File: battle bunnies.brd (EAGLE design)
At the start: 151.7 x 94 mm, 59 parts, among them IC1 CP2104, Q1 mmbt2222, Q2 mmbt2222, SW2 KMR2, U1 PCA9685, U2 SPX3819, U3 MCP73831T-2ACI/OT, X2 ESP-12, X4 20329

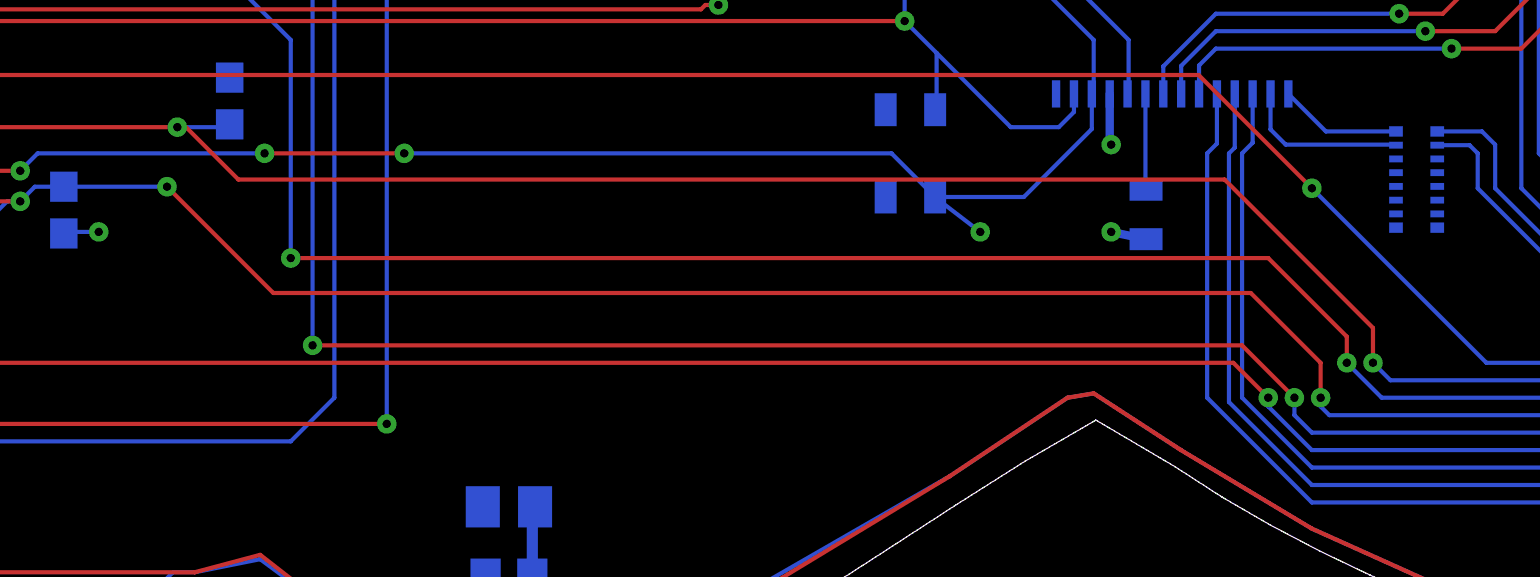
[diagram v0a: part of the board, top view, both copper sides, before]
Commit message: Fixing the trace that ran through the exposed ear
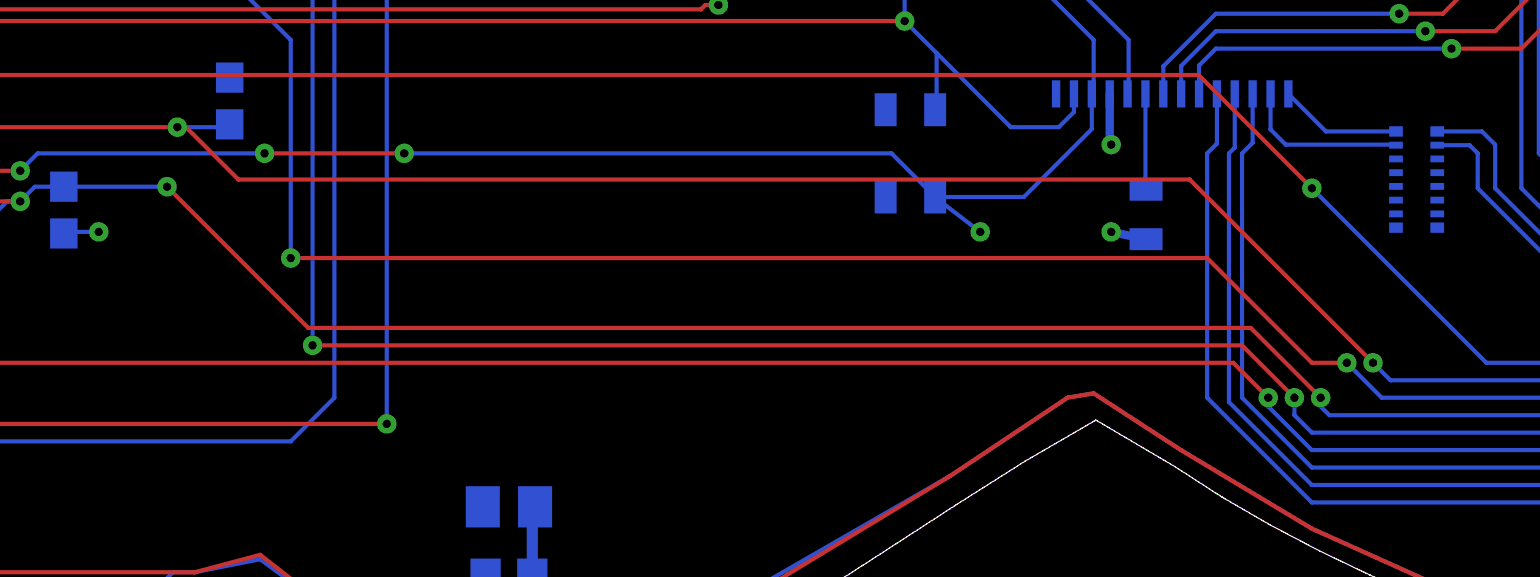
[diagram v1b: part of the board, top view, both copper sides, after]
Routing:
- net GPIO15: track 127.3 -> 126.6 mm
- net GPIO2: track 102.9 -> 102.2 mm
- net RESET: track 153.2 -> 152.6 mm
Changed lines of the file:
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@@
 <layer number="155" name="FabDoc3" color="7" fill="1" visible="yes" active="yes"/>
 <layer number="199" name="Contour" color="7" fill="1" visible="yes" active="yes"/>
-<layer number="200" name="200bmp" color="1" fill="10" visible="no" active="yes"/>
-<layer number="201" name="201bmp" color="2" fill="10" visible="no" active="yes"/>
-<layer number="202" name="202bmp" color="3" fill="10" visible="no" active="yes"/>
-<layer number="203" name="203bmp" color="4" fill="10" visible="no" active="yes"/>
-<layer number="204" name="204bmp" color="5" fill="10" visible="no" active="yes"/>
-<layer number="205" name="205bmp" color="6" fill="10" visible="no" active="yes"/>
-<layer number="206" name="206bmp" color="7" fill="10" visible="no" active="yes"/>
-<layer number="207" name="207bmp" color="8" fill="10" visible="no" active="yes"/>
-<layer number="208" name="208bmp" color="9" fill="10" visible="no" active="yes"/>
-<layer number="209" name="209bmp" color="10" fill="10" visible="no" active="yes"/>
-<layer number="210" name="210bmp" color="11" fill="10" visible="no" active="yes"/>
-<layer number="211" name="211bmp" color="12" fill="10" visible="no" active="yes"/>
-<layer number="212" name="212bmp" color="13" fill="10" visible="no" active="yes"/>
-<layer number="213" name="213bmp" color="14" fill="10" visible="no" active="yes"/>
-<layer number="214" name="214bmp" color="15" fill="10" visible="no" active="yes"/>
-<layer number="215" name="215bmp" color="16" fill="10" visible="no" active="yes"/>
-<layer number="216" name="216bmp" color="7" fill="1" visible="no" active="yes"/>
+<layer number="200" name="200bmp" color="1" fill="10" visible="yes" active="yes"/>
+<layer number="201" name="201bmp" color="2" fill="10" visible="yes" active="yes"/>
+<layer number="202" name="202bmp" color="3" fill="10" visible="yes" active="yes"/>
+<layer number="203" name="203bmp" color="4" fill="10" visible="yes" active="yes"/>
+<layer number="204" name="204bmp" color="5" fill="10" visible="yes" active="yes"/>
+<layer number="205" name="205bmp" color="6" fill="10" visible="yes" active="yes"/>
+<layer number="206" name="206bmp" color="7" fill="10" visible="yes" active="yes"/>
+<layer number="207" name="207bmp" color="8" fill="10" visible="yes" active="yes"/>
+<layer number="208" name="208bmp" color="9" fill="10" visible="yes" active="yes"/>
+<layer number="209" name="209bmp" color="10" fill="10" visible="yes" active="yes"/>
+<layer number="210" name="210bmp" color="11" fill="10" visible="yes" active="yes"/>
+<layer number="211" name="211bmp" color="12" fill="10" visible="yes" active="yes"/>
+<layer number="212" name="212bmp" color="13" fill="10" visible="yes" active="yes"/>
+<layer number="213" name="213bmp" color="14" fill="10" visible="yes" active="yes"/>
+<layer number="214" name="214bmp" color="15" fill="10" visible="yes" active="yes"/>
+<layer number="215" name="215bmp" color="16" fill="10" visible="yes" active="yes"/>
+<layer number="216" name="216bmp" color="7" fill="1" visible="yes" active="yes"/>
 <layer number="217" name="217bmp" color="18" fill="1" visible="no" active="no"/>
 <layer number="218" name="218bmp" color="19" fill="1" visible="no" active="no"/>
@@
 <layer number="223" name="223bmp" color="24" fill="1" visible="no" active="no"/>
 <layer number="224" name="224bmp" color="25" fill="1" visible="no" active="no"/>
-<layer number="225" name="225bmp" color="7" fill="1" visible="no" active="yes"/>
-<layer number="226" name="226bmp" color="7" fill="1" visible="no" active="yes"/>
-<layer number="227" name="227bmp" color="7" fill="1" visible="no" active="yes"/>
-<layer number="228" name="228bmp" color="7" fill="1" visible="no" active="yes"/>
-<layer number="229" name="229bmp" color="7" fill="1" visible="no" active="yes"/>
-<layer number="230" name="230bmp" color="7" fill="1" visible="no" active="yes"/>
-<layer number="231" name="231bmp" color="7" fill="1" visible="no" active="yes"/>
+<layer number="225" name="225bmp" color="7" fill="1" visible="yes" active="yes"/>
+<layer number="226" name="226bmp" color="7" fill="1" visible="yes" active="yes"/>
+<layer number="227" name="227bmp" color="7" fill="1" visible="yes" active="yes"/>
+<layer number="228" name="228bmp" color="7" fill="1" visible="yes" active="yes"/>
+<layer number="229" name="229bmp" color="7" fill="1" visible="yes" active="yes"/>
+<layer number="230" name="230bmp" color="7" fill="1" visible="yes" active="yes"/>
+<layer number="231" name="231bmp" color="7" fill="1" visible="yes" active="yes"/>
 <layer number="232" name="Eagle3D_PG2" color="7" fill="1" visible="no" active="no"/>
 <layer number="233" name="Eagle3D_PG3" color="7" fill="1" visible="no" active="no"/>
-<layer number="248" name="Housing" color="7" fill="1" visible="no" active="yes"/>
-<layer number="249" name="Edge" color="7" fill="1" visible="no" active="yes"/>
+<layer number="248" name="Housing" color="7" fill="1" visible="yes" active="yes"/>
+<layer number="249" name="Edge" color="7" fill="1" visible="yes" active="yes"/>
 <layer number="250" name="Descript" color="3" fill="1" visible="no" active="no"/>
 <layer number="251" name="SMDround" color="12" fill="11" visible="no" active="no"/>
-<layer number="254" name="cooling" color="7" fill="1" visible="no" active="yes"/>
-<layer number="255" name="routoute" color="7" fill="1" visible="no" active="yes"/>
+<layer number="254" name="cooling" color="7" fill="1" visible="yes" active="yes"/>
+<layer number="255" name="routoute" color="7" fill="1" visible="yes" active="yes"/>
 </layers>
 <board>
@@
 <wire x1="34.0925" y1="68.9525" x2="34.355" y2="69.215" width="0.1524" layer="1"/>
 <wire x1="55.245" y1="69.215" x2="45.4025" y2="69.215" width="0.1524" layer="16"/>
-<wire x1="100.33" y1="51.7525" x2="100.33" y2="50.8" width="0.1524" layer="1"/>
 <via x="100.33" y="50.8" extent="1-16" drill="0.3048" diameter="0.3048"/>
 <wire x1="100.33" y1="50.8" x2="101.6" y2="49.53" width="0.1524" layer="16"/>
 <wire x1="137.16" y1="44.45" x2="137.16" y2="41.91" width="0.1524" layer="16"/>
-<wire x1="61.9125" y1="54.61" x2="97.4725" y2="54.61" width="0.1524" layer="1"/>
-<wire x1="97.4725" y1="54.61" x2="100.33" y2="51.7525" width="0.1524" layer="1"/>
+<wire x1="61.9125" y1="54.61" x2="95.25" y2="54.61" width="0.1524" layer="1"/>
 <wire x1="101.6" y1="49.53" x2="128.27" y2="49.53" width="0.1524" layer="16"/>
 <wire x1="128.27" y1="49.53" x2="132.08" y2="45.72" width="0.1524" layer="16"/>
 <wire x1="132.08" y1="45.72" x2="135.89" y2="45.72" width="0.1524" layer="16"/>
 <wire x1="135.89" y1="45.72" x2="137.16" y2="44.45" width="0.1524" layer="16"/>
+<wire x1="100.33" y1="50.8" x2="99.06" y2="50.8" width="0.1524" layer="1"/>
+<wire x1="99.06" y1="50.8" x2="95.25" y2="54.61" width="0.1524" layer="1"/>
 </signal>
 <signal name="ADC">
@@
 <contactref element="JP2" pad="7"/>
 <wire x1="49.29" y1="57.15" x2="49.0925" y2="56.9525" width="0.1524" layer="1"/>
-<wire x1="99.3775" y1="50.8" x2="99.3775" y2="49.53" width="0.1524" layer="1"/>
 <via x="99.3775" y="49.53" extent="1-16" drill="0.3048" diameter="0.3048"/>
 <wire x1="99.3775" y1="49.53" x2="99.3775" y2="49.2125" width="0.1524" layer="16"/>
 <wire x1="99.3775" y1="49.2125" x2="99.695" y2="48.895" width="0.1524" layer="16"/>
-<wire x1="61.2775" y1="53.34" x2="96.8375" y2="53.34" width="0.1524" layer="1"/>
-<wire x1="96.8375" y1="53.34" x2="99.3775" y2="50.8" width="0.1524" layer="1"/>
 <wire x1="99.695" y1="48.895" x2="127.635" y2="48.895" width="0.1524" layer="16"/>
 <wire x1="127.635" y1="48.895" x2="132.08" y2="44.45" width="0.1524" layer="16"/>
-<wire x1="61.2775" y1="53.34" x2="57.41125" y2="57.20625" width="0.1524" layer="1"/>
+<wire x1="62.5475" y1="52.07" x2="57.41125" y2="57.20625" width="0.1524" layer="1"/>
 <wire x1="49.29" y1="57.15" x2="49.76625" y2="56.67375" width="0.1524" layer="1"/>
 <via x="52.07" y="56.67375" extent="1-16" drill="0.3048" diameter="0.3048"/>
@@
 <wire x1="45.72" y1="50.8" x2="51.59375" y2="56.67375" width="0.1524" layer="16"/>
 <wire x1="51.59375" y1="56.67375" x2="52.07" y2="56.67375" width="0.1524" layer="16"/>
+<wire x1="62.5475" y1="52.07" x2="96.8375" y2="52.07" width="0.1524" layer="1"/>
+<wire x1="96.8375" y1="52.07" x2="99.3775" y2="49.53" width="0.1524" layer="1"/>
 </signal>
 <signal name="GPIO0">
@@
 <wire x1="59.5875" y1="59.3725" x2="59.69" y2="59.475" width="0.1524" layer="16"/>
 <contactref element="JP2" pad="4"/>
-<wire x1="95.885" y1="57.4675" x2="60.0075" y2="57.4675" width="0.1524" layer="1"/>
+<wire x1="94.615" y1="57.4675" x2="60.0075" y2="57.4675" width="0.1524" layer="1"/>
 <wire x1="60.0075" y1="57.4675" x2="58.1025" y2="59.3725" width="0.1524" layer="1"/>
 <wire x1="58.1025" y1="59.3725" x2="57.785" y2="59.3725" width="0.1524" layer="1"/>
 <wire x1="49.5125" y1="59.3725" x2="49.0925" y2="58.9525" width="0.1524" layer="1"/>
-<wire x1="95.885" y1="57.4675" x2="101.2825" y2="52.07" width="0.1524" layer="1"/>
-<wire x1="101.2825" y1="52.07" x2="101.2825" y2="50.8" width="0.1524" layer="1"/>
 <via x="101.2825" y="50.8" extent="1-16" drill="0.3048" diameter="0.3048"/>
 <wire x1="101.2825" y1="50.8" x2="101.9175" y2="50.165" width="0.1524" layer="16"/>
@@
 <wire x1="132.08" y1="46.99" x2="138.43" y2="46.99" width="0.1524" layer="16"/>
 <wire x1="138.43" y1="46.99" x2="139.7" y2="45.72" width="0.1524" layer="16"/>
+<wire x1="101.2825" y1="50.8" x2="94.615" y2="57.4675" width="0.1524" layer="1"/>
 </signal>
 <signal name="GPIO14/SCK">

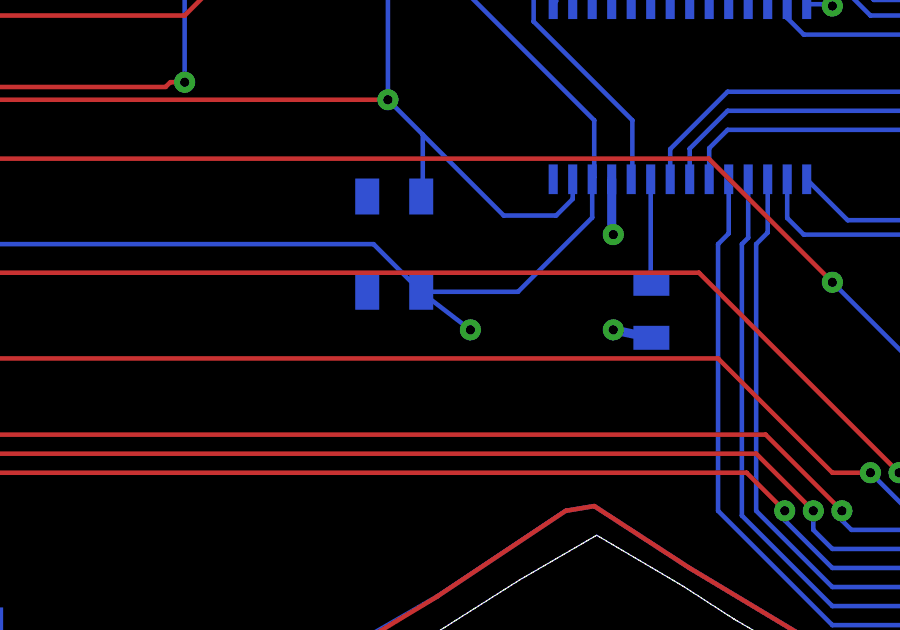
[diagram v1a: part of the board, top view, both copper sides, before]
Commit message: Removing extraneous via on GPIO14/SCK
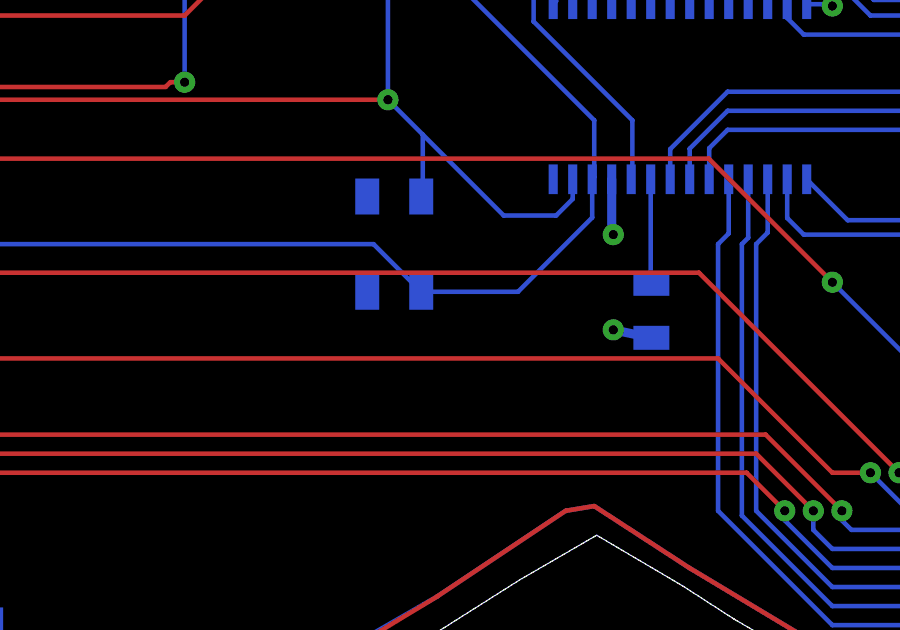
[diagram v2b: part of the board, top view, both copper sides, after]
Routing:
- net GPIO14/SCK: track 131.4 -> 129.4 mm, vias 5 -> 4
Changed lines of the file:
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@@
 <layer number="155" name="FabDoc3" color="7" fill="1" visible="yes" active="yes"/>
 <layer number="199" name="Contour" color="7" fill="1" visible="yes" active="yes"/>
-<layer number="200" name="200bmp" color="1" fill="10" visible="yes" active="yes"/>
-<layer number="201" name="201bmp" color="2" fill="10" visible="yes" active="yes"/>
-<layer number="202" name="202bmp" color="3" fill="10" visible="yes" active="yes"/>
-<layer number="203" name="203bmp" color="4" fill="10" visible="yes" active="yes"/>
-<layer number="204" name="204bmp" color="5" fill="10" visible="yes" active="yes"/>
-<layer number="205" name="205bmp" color="6" fill="10" visible="yes" active="yes"/>
-<layer number="206" name="206bmp" color="7" fill="10" visible="yes" active="yes"/>
-<layer number="207" name="207bmp" color="8" fill="10" visible="yes" active="yes"/>
-<layer number="208" name="208bmp" color="9" fill="10" visible="yes" active="yes"/>
-<layer number="209" name="209bmp" color="10" fill="10" visible="yes" active="yes"/>
-<layer number="210" name="210bmp" color="11" fill="10" visible="yes" active="yes"/>
-<layer number="211" name="211bmp" color="12" fill="10" visible="yes" active="yes"/>
-<layer number="212" name="212bmp" color="13" fill="10" visible="yes" active="yes"/>
-<layer number="213" name="213bmp" color="14" fill="10" visible="yes" active="yes"/>
-<layer number="214" name="214bmp" color="15" fill="10" visible="yes" active="yes"/>
-<layer number="215" name="215bmp" color="16" fill="10" visible="yes" active="yes"/>
-<layer number="216" name="216bmp" color="7" fill="1" visible="yes" active="yes"/>
+<layer number="200" name="200bmp" color="1" fill="10" visible="no" active="yes"/>
+<layer number="201" name="201bmp" color="2" fill="10" visible="no" active="yes"/>
+<layer number="202" name="202bmp" color="3" fill="10" visible="no" active="yes"/>
+<layer number="203" name="203bmp" color="4" fill="10" visible="no" active="yes"/>
+<layer number="204" name="204bmp" color="5" fill="10" visible="no" active="yes"/>
+<layer number="205" name="205bmp" color="6" fill="10" visible="no" active="yes"/>
+<layer number="206" name="206bmp" color="7" fill="10" visible="no" active="yes"/>
+<layer number="207" name="207bmp" color="8" fill="10" visible="no" active="yes"/>
+<layer number="208" name="208bmp" color="9" fill="10" visible="no" active="yes"/>
+<layer number="209" name="209bmp" color="10" fill="10" visible="no" active="yes"/>
+<layer number="210" name="210bmp" color="11" fill="10" visible="no" active="yes"/>
+<layer number="211" name="211bmp" color="12" fill="10" visible="no" active="yes"/>
+<layer number="212" name="212bmp" color="13" fill="10" visible="no" active="yes"/>
+<layer number="213" name="213bmp" color="14" fill="10" visible="no" active="yes"/>
+<layer number="214" name="214bmp" color="15" fill="10" visible="no" active="yes"/>
+<layer number="215" name="215bmp" color="16" fill="10" visible="no" active="yes"/>
+<layer number="216" name="216bmp" color="7" fill="1" visible="no" active="yes"/>
 <layer number="217" name="217bmp" color="18" fill="1" visible="no" active="no"/>
 <layer number="218" name="218bmp" color="19" fill="1" visible="no" active="no"/>
@@
 <layer number="223" name="223bmp" color="24" fill="1" visible="no" active="no"/>
 <layer number="224" name="224bmp" color="25" fill="1" visible="no" active="no"/>
-<layer number="225" name="225bmp" color="7" fill="1" visible="yes" active="yes"/>
-<layer number="226" name="226bmp" color="7" fill="1" visible="yes" active="yes"/>
-<layer number="227" name="227bmp" color="7" fill="1" visible="yes" active="yes"/>
-<layer number="228" name="228bmp" color="7" fill="1" visible="yes" active="yes"/>
-<layer number="229" name="229bmp" color="7" fill="1" visible="yes" active="yes"/>
-<layer number="230" name="230bmp" color="7" fill="1" visible="yes" active="yes"/>
-<layer number="231" name="231bmp" color="7" fill="1" visible="yes" active="yes"/>
+<layer number="225" name="225bmp" color="7" fill="1" visible="no" active="yes"/>
+<layer number="226" name="226bmp" color="7" fill="1" visible="no" active="yes"/>
+<layer number="227" name="227bmp" color="7" fill="1" visible="no" active="yes"/>
+<layer number="228" name="228bmp" color="7" fill="1" visible="no" active="yes"/>
+<layer number="229" name="229bmp" color="7" fill="1" visible="no" active="yes"/>
+<layer number="230" name="230bmp" color="7" fill="1" visible="no" active="yes"/>
+<layer number="231" name="231bmp" color="7" fill="1" visible="no" active="yes"/>
 <layer number="232" name="Eagle3D_PG2" color="7" fill="1" visible="no" active="no"/>
 <layer number="233" name="Eagle3D_PG3" color="7" fill="1" visible="no" active="no"/>
-<layer number="248" name="Housing" color="7" fill="1" visible="yes" active="yes"/>
-<layer number="249" name="Edge" color="7" fill="1" visible="yes" active="yes"/>
+<layer number="248" name="Housing" color="7" fill="1" visible="no" active="yes"/>
+<layer number="249" name="Edge" color="7" fill="1" visible="no" active="yes"/>
 <layer number="250" name="Descript" color="3" fill="1" visible="no" active="no"/>
 <layer number="251" name="SMDround" color="12" fill="11" visible="no" active="no"/>
-<layer number="254" name="cooling" color="7" fill="1" visible="yes" active="yes"/>
+<layer number="254" name="cooling" color="7" fill="1" visible="no" active="yes"/>
 <layer number="255" name="routoute" color="7" fill="1" visible="yes" active="yes"/>
 </layers>
@@
 <wire x1="8.89" y1="74.93" x2="5.715" y2="74.93" width="0.1524" layer="1"/>
 <wire x1="16.8275" y1="68.58" x2="15.24" y2="70.1675" width="0.1524" layer="1"/>
-<wire x1="15.24" y1="70.1675" x2="13.6525" y2="70.1675" width="0.1524" layer="1"/>
 <wire x1="13.6525" y1="70.1675" x2="8.89" y2="74.93" width="0.1524" layer="1"/>
 <wire x1="16.8275" y1="68.58" x2="20.32" y2="68.58" width="0.1524" layer="1"/>
@@
 <wire x1="120.65" y1="48.26" x2="121.92" y2="46.99" width="0.1524" layer="16"/>
 <wire x1="121.92" y1="46.99" x2="121.92" y2="41.91" width="0.1524" layer="16"/>
+<wire x1="15.24" y1="70.1675" x2="13.6525" y2="70.1675" width="0.1524" layer="1"/>
 </signal>
 <signal name="GPIO4/SDA">
@@
 <wire x1="133.0325" y1="84.1375" x2="133.0325" y2="87.3125" width="0.1524" layer="1"/>
 <wire x1="88.5825" y1="56.8325" x2="85.355" y2="56.8325" width="0.1524" layer="16"/>
-<via x="86.995" y="55.5625" extent="1-16" drill="0.3048"/>
-<wire x1="85.355" y1="56.8325" x2="85.4075" y2="56.78" width="0.1524" layer="16"/>
-<wire x1="85.4075" y1="56.78" x2="86.995" y2="55.5625" width="0.1524" layer="16"/>
 <wire x1="42.545" y1="57.785" x2="39.3775" y2="60.9525" width="0.1524" layer="1"/>
 <wire x1="39.3775" y1="60.9525" x2="34.0925" y2="60.9525" width="0.1524" layer="1"/>
